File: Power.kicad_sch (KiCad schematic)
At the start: 42 parts, among them J3 U263-163N-4OS1735, Q1 YJQ10N02A, Q2 YJQ10N02A, Q3 YJQD30P02A, SW7 Power, U4 XC6210B332MR, U5 LGS4056H, U6 SSP61CC3602MR, U7 XC6206P182MR

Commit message: Did some things
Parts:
- C43: value 0.1uF -> 100nF
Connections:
- net BATT+: no longer R33.1
- net Batt+_unfuse: now also BT1.2 (+); no longer BT1.1 (+)
- net Vin: now also R33.1
- net at Q1.3 (D): now also BT1.1; no longer BT1.2 (-)
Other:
- note added: "10uF GRT188R60J106ME13 1uF GRM155R61E105KA12D"
- note removed: "10uF GRM188R60J106ME84 1uF GRM155R61E105KA12D"
- note removed: "1200mah battery"
- note removed: "https://www.aliexpress.com/item/32897762803.html"

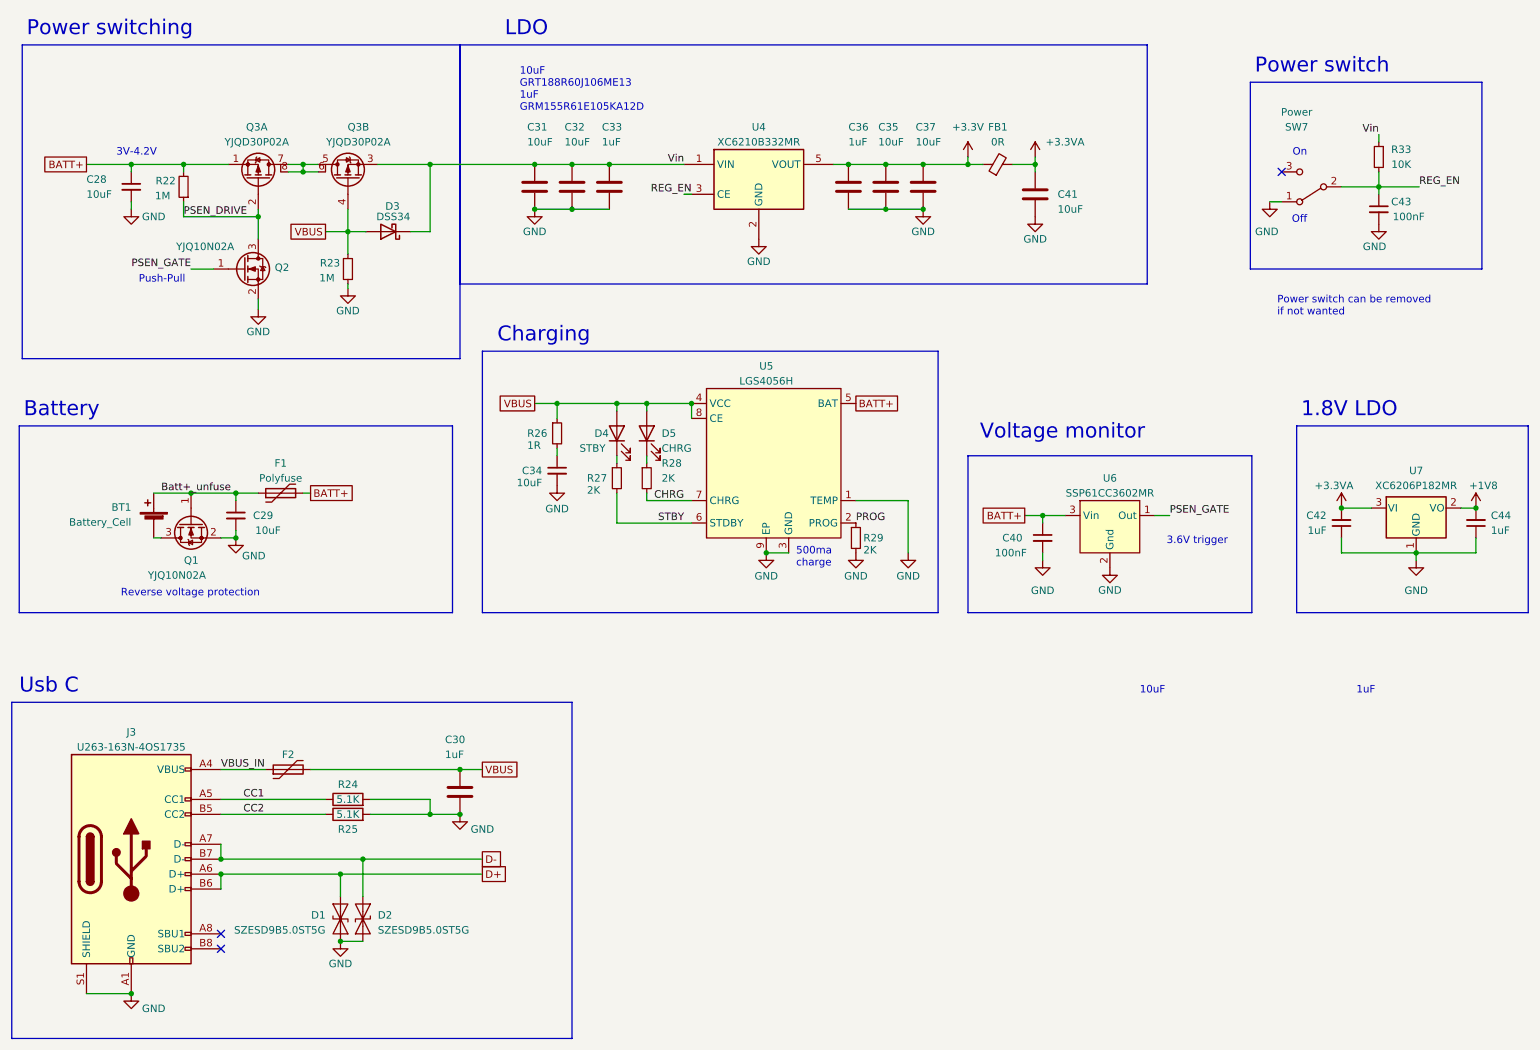
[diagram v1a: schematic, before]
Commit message: Removed slashes from filenames
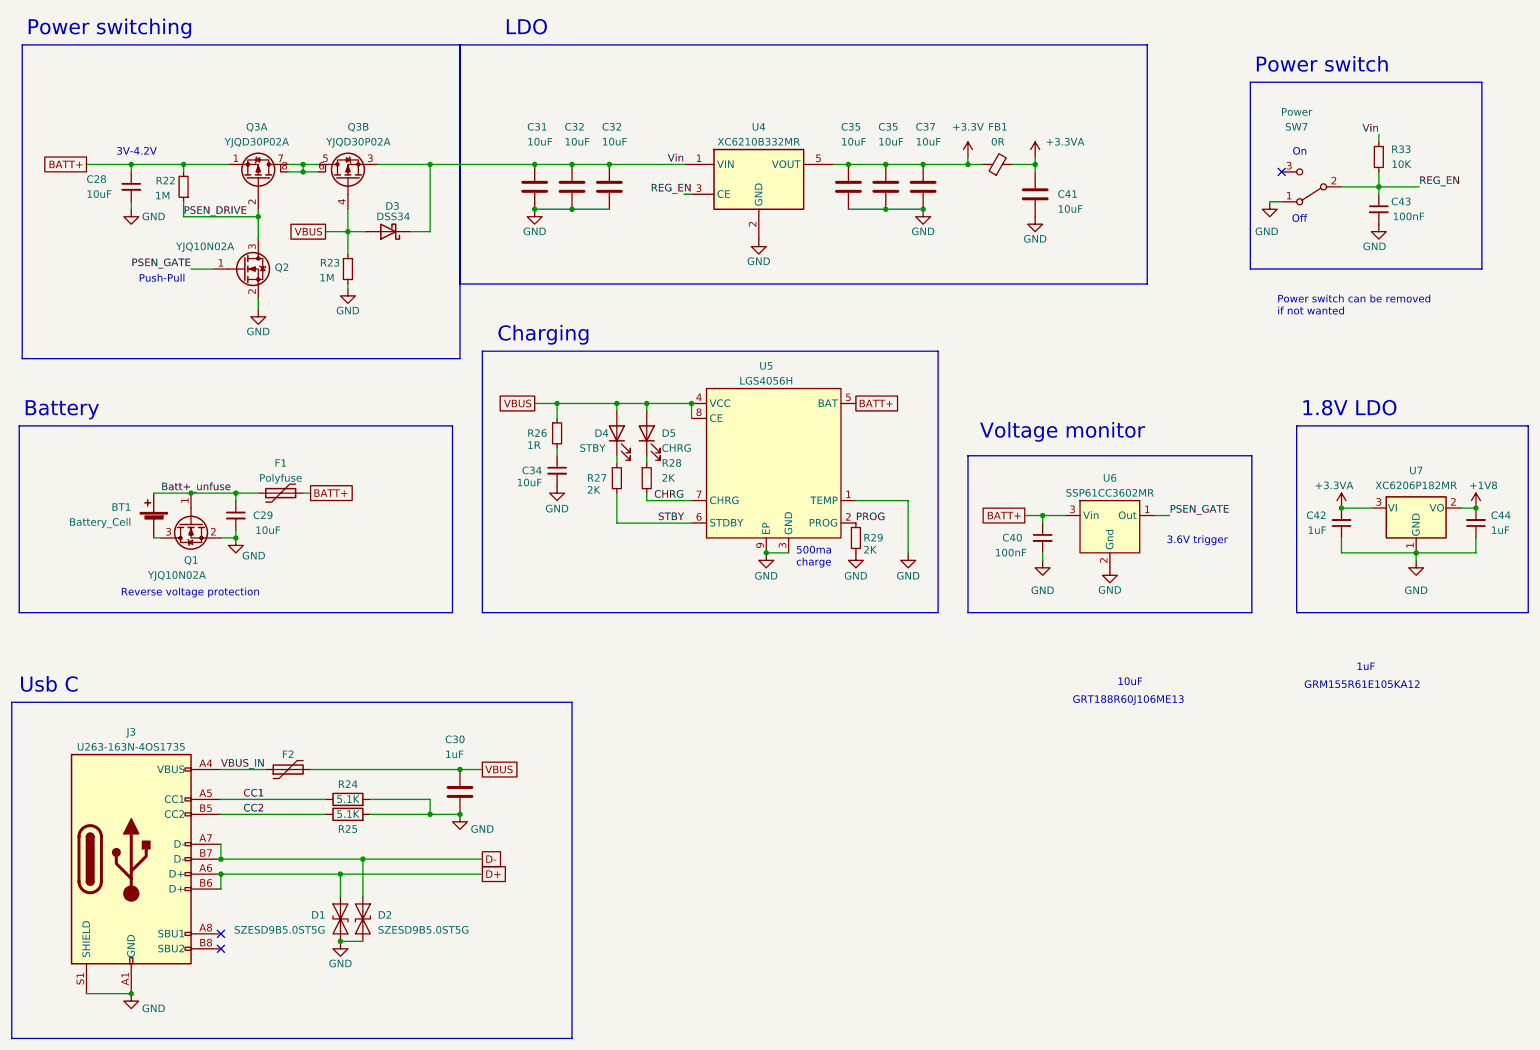
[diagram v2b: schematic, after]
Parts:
- removed C33, C36: 1uF, Capacitor_SMD:C_0402_1005Metric, symbol Device:C
- added C32, C35: 10uF, Capacitor_SMD:C_0603_1608Metric, symbol Device:C
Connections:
- net +3.3V: now also C35.1
- net GND: now also C32.2, C35.2
- net Vin: now also C32.1
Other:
- note added: "GRM155R61E105KA12"
- note added: "GRT188R60J106ME13"
- note removed: "10uF GRT188R60J106ME13 1uF GRM155R61E105KA12D"
